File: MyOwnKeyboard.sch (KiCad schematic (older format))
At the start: 346 parts

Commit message: Assigned switches Romer-G footprint
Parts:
- SW1, SW10, SW100, SW101, SW102, SW103, SW104, SW105, SW106, SW107, SW108, SW109, SW11, SW110, SW111, SW112, SW113, SW114, SW115, SW116, SW117, SW118, SW119, SW12, SW120, SW121, SW122, SW123, SW124, SW125, SW126, SW127, SW128, SW129, SW13, SW130, SW131, SW132, SW133, SW134, SW135, SW136, SW137, SW138, SW139, SW14, SW140, SW141, SW142, SW143, SW144, SW145, SW146, SW147, SW148, SW149, SW15, SW150, SW151, SW152, SW153, SW154, SW155, SW156, SW157, SW158, SW159, SW16, SW160, SW161, SW162, SW163, SW164, SW165, SW166, SW167, SW168, SW169, SW17, SW170, SW171, SW172, SW173, SW174, SW175, SW176, SW177, SW178, SW179, SW18, SW180, SW181, SW182, SW183, SW184, SW185, SW186, SW187, SW188, SW189, SW19, SW190, SW191, SW192, SW193, SW194, SW195, SW196, SW197, SW198, SW199, SW2, SW20, SW200, SW201, SW202, SW203, SW204, SW205, SW206, SW207, SW208, SW209, SW21, SW210, SW211, SW212, SW213, SW214, SW215, SW216, SW217, SW218, SW219, SW22, SW220, SW221, SW222, SW223, SW224, SW225, SW226, SW227, SW228, SW23, SW24, SW25, SW26, SW27, SW28, SW29, SW3, SW30, SW31, SW32, SW33, SW34, SW35, SW36, SW37, SW38, SW39, SW4, SW40, SW41, SW42, SW43, SW44, SW45, SW46, SW47, SW48, SW49, SW5, SW50, SW51, SW52, SW53, SW54, SW55, SW56, SW57, SW58, SW59, SW6, SW60, SW61, SW62, SW63, SW64, SW65, SW66, SW67, SW68, SW69, SW7, SW70, SW71, SW72, SW73, SW74, SW75, SW76, SW77, SW78, SW79, SW8, SW80, SW81, SW82, SW83, SW84, SW85, SW86, SW87, SW88, SW89, SW9, SW90, SW91, SW92, SW93, SW94, SW95, SW96, SW97, SW98, SW99: renamed from SW?; footprint (none) -> MyOwnKeyboard:RomerG
- gave numbers to parts that had none: 118

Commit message: Migrate to the ATMega164
Why use IO expanders when you can just get more pins. It still turns out ~$3 cheaper.
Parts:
- removed SW1, SW10, SW100, SW101, SW102, SW103, SW104, SW105, SW106, SW107, SW108, SW109, SW11, SW110, SW111, SW112, SW113, SW114, SW12, SW13, SW14, SW15, SW16, SW17, SW18, SW19, SW2, SW20, SW21, SW22, SW23, SW24, SW25, SW26, SW27, SW28, SW29, SW3, SW30, SW31, SW32, SW33, SW34, SW35, SW36, SW37, SW38, SW39, SW4, SW40, SW41, SW42, SW43, SW44, SW45, SW46, SW47, SW48, SW49, SW5, SW50, SW51, SW52, SW53, SW54, SW55, SW56, SW57, SW58, SW59, SW6, SW60, SW61, SW62, SW63, SW64, SW65, SW66, SW67, SW68, SW69, SW7, SW70, SW71, SW72, SW73, SW74, SW75, SW76, SW77, SW78, SW79, SW8, SW80, SW81, SW82, SW83, SW84, SW85, SW86, SW87, SW88, SW89, SW9, SW90, SW91, SW92, SW93, SW94, SW95, SW96, SW97, SW98, SW99: SW_SPST, MyOwnKeyboard:RomerG, symbol Switch:SW_SPST
- removed U1: ATtiny85-20PU, Package_DIP:DIP-8_W7.62mm, symbol MCU_Microchip_ATtiny:ATtiny85-20PU
- removed U2, U3: MCP23017_SP, Package_DIP:DIP-28_W7.62mm, symbol Interface_Expansion:MCP23017_SP
- added C1, C2: 30pF, symbol Device:CP1
- added D115, D116, D117: LED, symbol Device:LED
- added Q1: 2N7000, Package_TO_SOT_THT:TO-92_Inline, symbol Transistor_FET:2N7000
- added R1: 100, symbol Device:R
- added R2: 100k, symbol Device:R
- added R3, R4, R5: 150, symbol Device:R
- added U1: ATmega164P-20PU, Package_DIP:DIP-40_W15.24mm, symbol MCU_Microchip_ATmega:ATmega164P-20PU
- added Y1: 20MHz, Crystal:Crystal_HC49-U_Horizontal, symbol Device:Crystal
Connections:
- net labels added: Counter2A-PWM
- net labels removed: SCL, SDA
- wire segments 1151 -> 616
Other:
- note removed: "I2C"
- note removed: "PS/2"
- moved on the sheet: J1

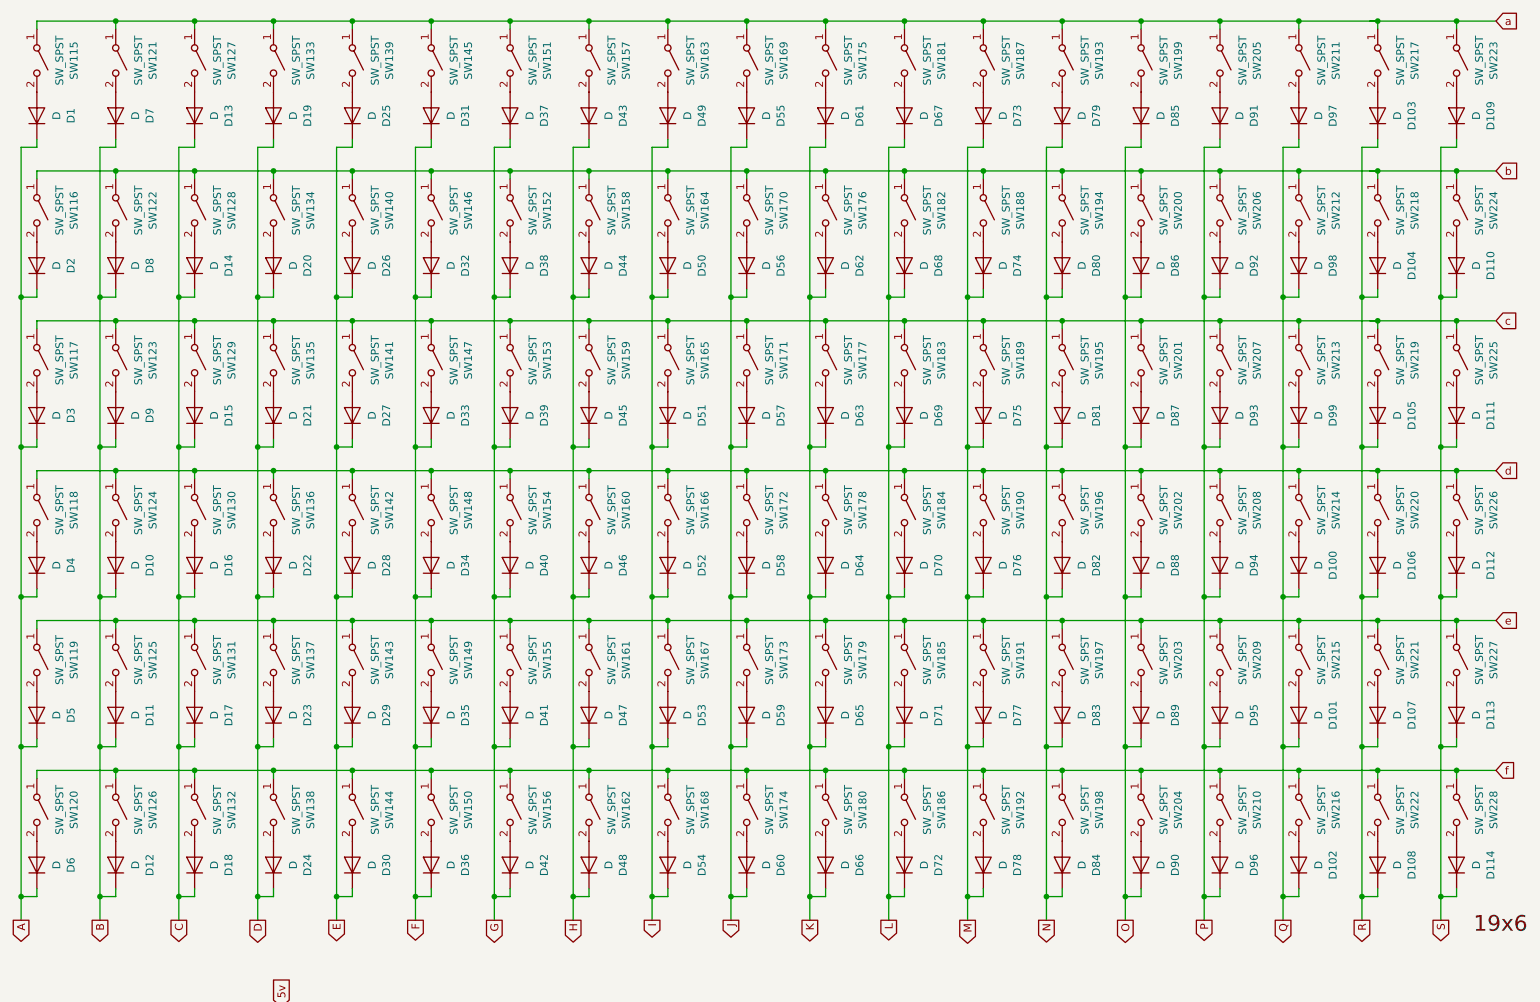
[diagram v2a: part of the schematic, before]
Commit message: Add LED and assign footprints
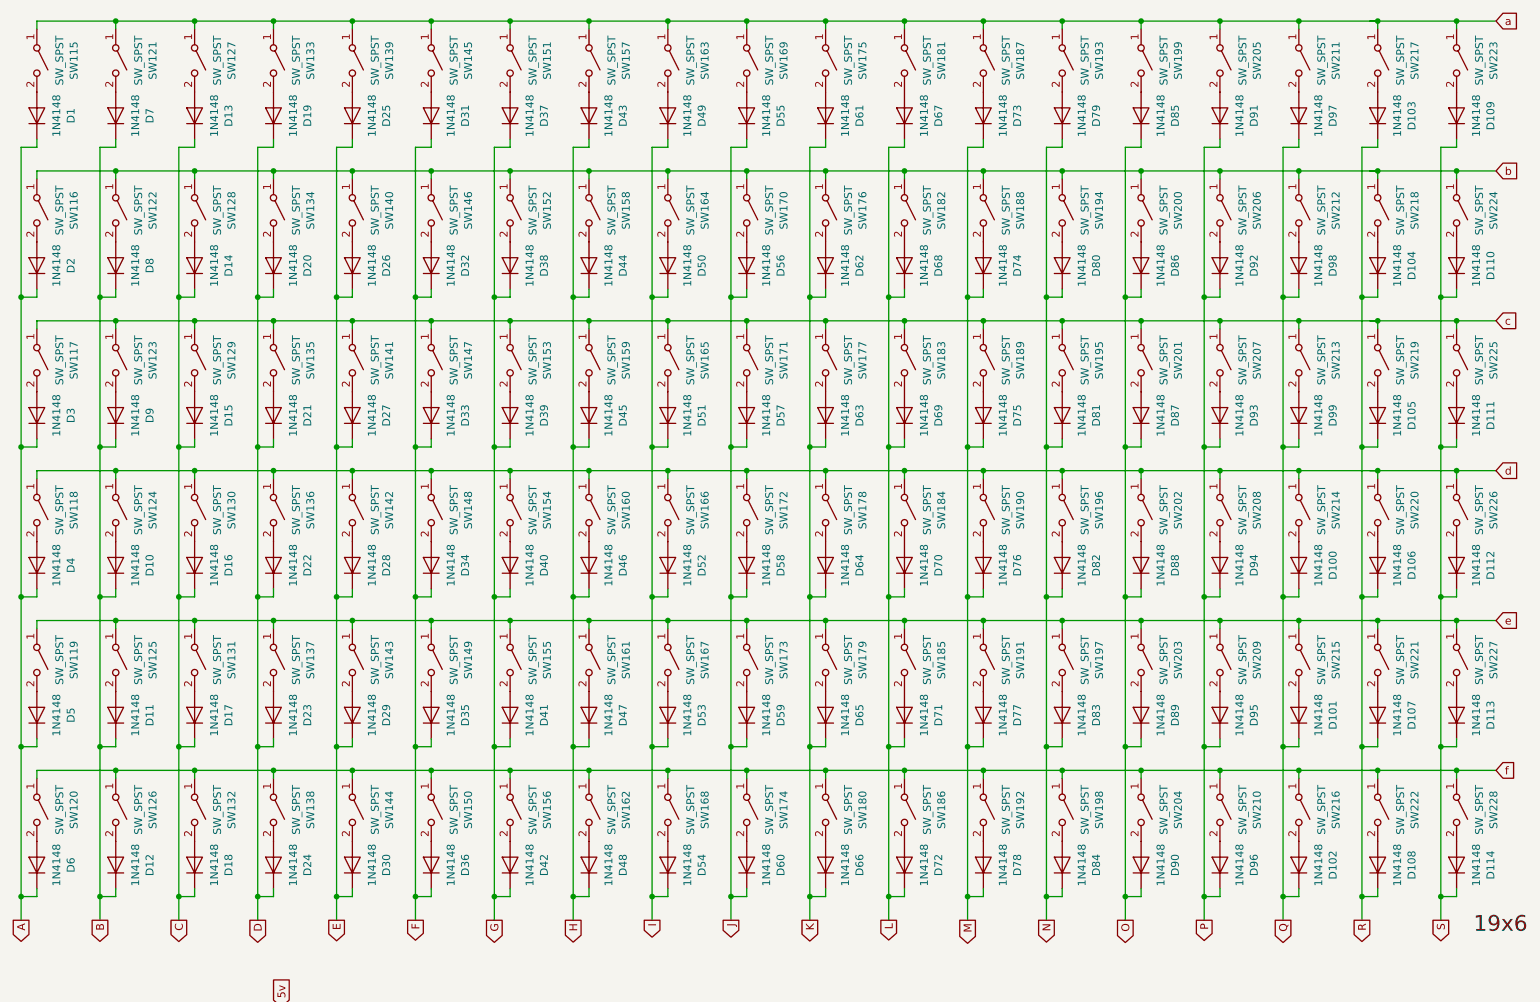
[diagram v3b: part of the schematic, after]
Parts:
- D1, D10, D100, D101, D102, D103, D104, D105, D106, D107, D108, D109, D11, D110, D111, D112, D113, D114, D12, D13, D14, D15, D16, D17, D18, D19, D2, D20, D21, D22, D23, D24, D25, D26, D27, D28, D29, D3, D30, D31, D32, D33, D34, D35, D36, D37, D38, D39, D4, D40, D41, D42, D43, D44, D45, D46, D47, D48, D49, D5, D50, D51, D52, D53, D54, D55, D56, D57, D58, D59, D6, D60, D61, D62, D63, D64, D65, D66, D67, D68, D69, D7, D70, D71, D72, D73, D74, D75, D76, D77, D78, D79, D8, D80, D81, D82, D83, D84, D85, D86, D87, D88, D89, D9, D90, D91, D92, D93, D94, D95, D96, D97, D98, D99: value D -> 1N4148; footprint (none) -> Diode_THT:D_DO-35_SOD27_P7.62mm_Horizontal
- D115, D116, D117: footprint (none) -> MyOwnKeyboard:158301250
- R1, R2, R3, R4, R5: footprint (none) -> Resistor_SMD:R_0805_2012Metric_Pad1.15x1.40mm_HandSolder

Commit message: Add per-key LEDs, basic PCB layout
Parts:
- added D118, D119, D120, D121, D122, D123, D124, D125, D126, D127, D128, D129, D130, D131, D132, D133, D134, D135, D136, D137, D138, D139, D140, D141, D142, D143, D144, D145, D146, D147, D148, D149, D150, D151, D152, D153, D154, D155, D156, D157, D158, D159, D160, D161, D162, D163, D164, D165, D166, D167, D168, D169, D170, D171, D172, D173, D174, D175, D176, D177, D178, D179, D180, D181, D182, D183, D184, D185, D186, D187, D188, D189, D190, D191, D192, D193, D194, D195, D196, D197, D198, D199, D200, D201, D202, D203, D204, D205, D206, D207, D208, D209, D210, D211, D212, D213, D214, D215, D216, D217, D218, D219, D220, D221, D222, D223, D224, D225, D226, D227, D228: LED, MyOwnKeyboard:158301250, symbol Device:LED
- added R10, R100, R101, R102, R103, R104, R105, R106, R107, R108, R109, R11, R110, R111, R112, R113, R114, R115, R116, R12, R13, R14, R15, R16, R17, R18, R19, R20, R21, R22, R23, R24, R25, R26, R27, R28, R29, R30, R31, R32, R33, R34, R35, R36, R37, R38, R39, R40, R41, R42, R43, R44, R45, R46, R47, R48, R49, R50, R51, R52, R53, R54, R55, R56, R57, R58, R59, R6, R60, R61, R62, R63, R64, R65, R66, R67, R68, R69, R7, R70, R71, R72, R73, R74, R75, R76, R77, R78, R79, R8, R80, R81, R82, R83, R84, R85, R86, R87, R88, R89, R9, R90, R91, R92, R93, R94, R95, R96, R97, R98, R99: 2.3k, Resistor_SMD:R_0805_2012Metric_Pad1.15x1.40mm_HandSolder, symbol Device:R
- R3, R4, R5: value 150 -> 2.3k
- renumbered D55 to D10, D30 to D100, D36 to D101, D42 to D102, D48 to D103, D54 to D104, D60 to D105, D66 to D106, D72 to D107, D78 to D108, D84 to D109, D61 to D11, D90 to D110, D96 to D111, D102 to D112, D108 to D113, D67 to D12, D73 to D13, D79 to D14, D85 to D15, D91 to D16, D97 to D17, D103 to D18, D109 to D19, D7 to D2, D2 to D20, D8 to D21, D14 to D22, D20 to D23, D26 to D24, D32 to D25, D38 to D26, D44 to D27, D50 to D28, D56 to D29, D13 to D3, D62 to D30, D68 to D31, D74 to D32, D80 to D33, D86 to D34, D92 to D35, D98 to D36, D104 to D37, D110 to D38, D3 to D39, D19 to D4, D9 to D40, D15 to D41, D21 to D42, D27 to D43, D33 to D44, D39 to D45, D45 to D46, D51 to D47, D57 to D48, D63 to D49, D25 to D5, D69 to D50, D75 to D51, D81 to D52, D87 to D53, D93 to D54, D99 to D55, D105 to D56, D111 to D57, D4 to D58, D10 to D59, D31 to D6, D16 to D60, D22 to D61, D28 to D62, D34 to D63, D40 to D64, D46 to D65, D52 to D66, D58 to D67, D64 to D68, D70 to D69, D37 to D7, D76 to D70, D82 to D71, D88 to D72, D94 to D73, D100 to D74, D106 to D75, D112 to D76, D5 to D77, D11 to D78, D17 to D79, D43 to D8, D23 to D80, D29 to D81, D35 to D82, D41 to D83, D47 to D84, D53 to D85, D59 to D86, D65 to D87, D71 to D88, D77 to D89, D49 to D9, D83 to D90, D89 to D91, D95 to D92, D101 to D93, D107 to D94, D113 to D95, D6 to D96, D12 to D97, D18 to D98, D24 to D99, SW115 to SW1, SW169 to SW10, SW144 to SW100, SW150 to SW101, SW156 to SW102, SW162 to SW103, SW168 to SW104, SW174 to SW105, SW180 to SW106, SW186 to SW107, SW192 to SW108, SW198 to SW109, SW175 to SW11, SW204 to SW110, SW210 to SW111, SW216 to SW112, SW222 to SW113, SW228 to SW114, SW181 to SW12, SW187 to SW13, SW193 to SW14, SW199 to SW15, SW205 to SW16, SW211 to SW17, SW217 to SW18, SW223 to SW19, SW121 to SW2, SW116 to SW20, SW122 to SW21, SW128 to SW22, SW134 to SW23, SW140 to SW24, SW146 to SW25, SW152 to SW26, SW158 to SW27, SW164 to SW28, SW170 to SW29, SW127 to SW3, SW176 to SW30, SW182 to SW31, SW188 to SW32, SW194 to SW33, SW200 to SW34, SW206 to SW35, SW212 to SW36, SW218 to SW37, SW224 to SW38, SW117 to SW39, SW133 to SW4, SW123 to SW40, SW129 to SW41, SW135 to SW42, SW141 to SW43, SW147 to SW44, SW153 to SW45, SW159 to SW46, SW165 to SW47, SW171 to SW48, SW177 to SW49, SW139 to SW5, SW183 to SW50, SW189 to SW51, SW195 to SW52, SW201 to SW53, SW207 to SW54, SW213 to SW55, SW219 to SW56, SW225 to SW57, SW118 to SW58, SW124 to SW59, SW145 to SW6, SW130 to SW60, SW136 to SW61, SW142 to SW62, SW148 to SW63, SW154 to SW64, SW160 to SW65, SW166 to SW66, SW172 to SW67, SW178 to SW68, SW184 to SW69, SW151 to SW7, SW190 to SW70, SW196 to SW71, SW202 to SW72, SW208 to SW73, SW214 to SW74, SW220 to SW75, SW226 to SW76, SW119 to SW77, SW125 to SW78, SW131 to SW79, SW157 to SW8, SW137 to SW80, SW143 to SW81, SW149 to SW82, SW155 to SW83, SW161 to SW84, SW167 to SW85, SW173 to SW86, SW179 to SW87, SW185 to SW88, SW191 to SW89, SW163 to SW9, SW197 to SW90, SW203 to SW91, SW209 to SW92, SW215 to SW93, SW221 to SW94, SW227 to SW95, SW120 to SW96, SW126 to SW97, SW132 to SW98, SW138 to SW99
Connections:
- net 5v: now also R3.1, R4.1, R5.1, R10.1, R100.1, R101.1, R102.1, R103.1, R104.1, R105.1, R106.1, R107.1, R108.1, R109.1, R11.1, R110.1, R111.1, R112.1, R113.1, R114.1, R115.1, R116.1, R12.1, R13.1, R14.1, R15.1, R16.1, R17.1, R18.1, R19.1, R20.1, R21.1, R22.1, R23.1, R24.1, R25.1, R26.1, R27.1, R28.1, R29.1, R30.1, R31.1, R32.1, R33.1, R34.1, R35.1, R36.1, R37.1, R38.1, R39.1, R40.1, R41.1, R42.1, R43.1, R44.1, R45.1, R46.1, R47.1, R48.1, R49.1, R50.1, R51.1, R52.1, R53.1, R54.1, R55.1, R56.1, R57.1, R58.1, R59.1, R6.1, R60.1, R61.1, R62.1, R63.1, R64.1, R65.1, R66.1, R67.1, R68.1, R69.1, R7.1, R70.1, R71.1, R72.1, R73.1, R74.1, R75.1, R76.1, R77.1, R78.1, R79.1, R8.1, R80.1, R81.1, R82.1, R83.1, R84.1, R85.1, R86.1, R87.1, R88.1, R89.1, R9.1, R90.1, R91.1, R92.1, R93.1, R94.1, R95.1, R96.1, R97.1, R98.1, R99.1; no longer R3.2, R4.2, R5.2
- net Counter2A-PWM: now also R1.1; no longer R1.2
- net at D115.1 (K), D116.1 (K), D117.1 (K)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: now also D118.1 (K), D119.1 (K), D120.1 (K), D121.1 (K), D122.1 (K), D123.1 (K), D124.1 (K), D125.1 (K), D126.1 (K), D127.1 (K), D128.1 (K), D129.1 (K), D130.1 (K), D131.1 (K), D132.1 (K), D133.1 (K), D134.1 (K), D135.1 (K), D136.1 (K), D137.1 (K), D138.1 (K), D139.1 (K), D140.1 (K), D141.1 (K), D142.1 (K), D143.1 (K), D144.1 (K), D145.1 (K), D146.1 (K), D147.1 (K), D148.1 (K), D149.1 (K), D150.1 (K), D151.1 (K), D152.1 (K), D153.1 (K), D154.1 (K), D155.1 (K), D156.1 (K), D157.1 (K), D158.1 (K), D159.1 (K), D160.1 (K), D161.1 (K), D162.1 (K), D163.1 (K), D164.1 (K), D165.1 (K), D166.1 (K), D167.1 (K), D168.1 (K), D169.1 (K), D170.1 (K), D171.1 (K), D172.1 (K), D173.1 (K), D174.1 (K), D175.1 (K), D176.1 (K), D177.1 (K), D178.1 (K), D179.1 (K), D180.1 (K), D181.1 (K), D182.1 (K), D183.1 (K), D184.1 (K), D185.1 (K), D186.1 (K), D187.1 (K), D188.1 (K), D189.1 (K), D190.1 (K), D191.1 (K), D192.1 (K), D193.1 (K), D194.1 (K), D195.1 (K), D196.1 (K), D197.1 (K), D198.1 (K), D199.1 (K), D200.1 (K), D201.1 (K), D202.1 (K), D203.1 (K), D204.1 (K), D205.1 (K), D206.1 (K), D207.1 (K), D208.1 (K), D209.1 (K), D210.1 (K), D211.1 (K), D212.1 (K), D213.1 (K), D214.1 (K), D215.1 (K), D216.1 (K), D217.1 (K), D218.1 (K), D219.1 (K), D220.1 (K), D221.1 (K), D222.1 (K), D223.1 (K), D224.1 (K), D225.1 (K), D226.1 (K), D227.1 (K), D228.1 (K)
- net at D117.2 (A): now also R5.2; no longer R5.1
- net at D116.2 (A): now also R4.2; no longer R4.1
- net at D115.2 (A): now also R3.2; no longer R3.1
- net at Q1.2 (G), R2.1: now also R1.2; no longer R1.1
- new net: D134.2 (A), R22.2
- new net: D153.2 (A), R41.2
- new net: D172.2 (A), R60.2
- new net: D191.2 (A), R79.2
- new net: D210.2 (A), R98.2
- new net: D135.2 (A), R23.2
- new net: D154.2 (A), R42.2
- new net: D173.2 (A), R61.2
- new net: D192.2 (A), R80.2
- new net: D211.2 (A), R99.2
- new net: D136.2 (A), R24.2
- new net: D155.2 (A), R43.2
- new net: D174.2 (A), R62.2
- new net: D193.2 (A), R81.2
- new net: D212.2 (A), R100.2
- new net: D118.2 (A), R6.2
- new net: D137.2 (A), R25.2
- new net: D156.2 (A), R44.2
- new net: D175.2 (A), R63.2
- new net: D194.2 (A), R82.2
- new net: D213.2 (A), R101.2
- new net: D119.2 (A), R7.2
- new net: D138.2 (A), R26.2
- new net: D157.2 (A), R45.2
- new net: D176.2 (A), R64.2
- new net: D195.2 (A), R83.2
- new net: D214.2 (A), R102.2
- new net: D120.2 (A), R8.2
- new net: D139.2 (A), R27.2
- new net: D158.2 (A), R46.2
- new net: D177.2 (A), R65.2
- new net: D196.2 (A), R84.2
- new net: D215.2 (A), R103.2
- new net: D121.2 (A), R9.2
- new net: D140.2 (A), R28.2
- new net: D159.2 (A), R47.2
- new net: D178.2 (A), R66.2
- new net: D197.2 (A), R85.2
- new net: D216.2 (A), R104.2
- new net: D122.2 (A), R10.2
- new net: D141.2 (A), R29.2
- new net: D160.2 (A), R48.2
- new net: D179.2 (A), R67.2
- new net: D198.2 (A), R86.2
- new net: D217.2 (A), R105.2
- new net: D123.2 (A), R11.2
- new net: D142.2 (A), R30.2
- new net: D161.2 (A), R49.2
- new net: D180.2 (A), R68.2
- new net: D199.2 (A), R87.2
- new net: D218.2 (A), R106.2
- new net: D124.2 (A), R12.2
- new net: D143.2 (A), R31.2
- new net: D162.2 (A), R50.2
- new net: D181.2 (A), R69.2
- new net: D200.2 (A), R88.2
- new net: D219.2 (A), R107.2
- new net: D125.2 (A), R13.2
- new net: D144.2 (A), R32.2
- new net: D163.2 (A), R51.2
- new net: D182.2 (A), R70.2
- new net: D201.2 (A), R89.2
- new net: D220.2 (A), R108.2
- new net: D126.2 (A), R14.2
- new net: D145.2 (A), R33.2
- new net: D164.2 (A), R52.2
- new net: D183.2 (A), R71.2
- new net: D202.2 (A), R90.2
- new net: D221.2 (A), R109.2
- new net: D127.2 (A), R15.2
- new net: D146.2 (A), R34.2
- new net: D165.2 (A), R53.2
- new net: D184.2 (A), R72.2
- new net: D203.2 (A), R91.2
- new net: D222.2 (A), R110.2
- new net: D128.2 (A), R16.2
- new net: D147.2 (A), R35.2
- new net: D166.2 (A), R54.2
- new net: D185.2 (A), R73.2
- new net: D204.2 (A), R92.2
- new net: D223.2 (A), R111.2
- new net: D129.2 (A), R17.2
- new net: D148.2 (A), R36.2
- new net: D167.2 (A), R55.2
- new net: D186.2 (A), R74.2
- new net: D205.2 (A), R93.2
- new net: D224.2 (A), R112.2
- new net: D130.2 (A), R18.2
- new net: D149.2 (A), R37.2
- new net: D168.2 (A), R56.2
- new net: D187.2 (A), R75.2
- new net: D206.2 (A), R94.2
- new net: D225.2 (A), R113.2
- new net: D131.2 (A), R19.2
- new net: D150.2 (A), R38.2
- new net: D169.2 (A), R57.2
- new net: D188.2 (A), R76.2
- new net: D207.2 (A), R95.2
- new net: D226.2 (A), R114.2
- new net: D132.2 (A), R20.2
- new net: D151.2 (A), R39.2
- new net: D170.2 (A), R58.2
- new net: D189.2 (A), R77.2
- new net: D208.2 (A), R96.2
- new net: D227.2 (A), R115.2
- new net: D133.2 (A), R21.2
- new net: D152.2 (A), R40.2
- new net: D171.2 (A), R59.2
- new net: D190.2 (A), R78.2
- new net: D209.2 (A), R97.2
- new net: D228.2 (A), R116.2
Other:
- moved on the sheet: C1, C2, D1, D10, D100, D101, D102, D103, D104, D105, D106, D107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

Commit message: Add NUM/CAPSLOCK indicators, finalise components
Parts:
- added D229: NUMLOCK, MyOwnKeyboard:158301250, symbol Device:LED
- added D230: CAPSLOCK, MyOwnKeyboard:158301250, symbol Device:LED
- added R117, R118: 2.3k, Resistor_SMD:R_0805_2012Metric_Pad1.15x1.40mm_HandSolder, symbol Device:R
- C1, C2: footprint (none) -> Capacitor_SMD:C_0805_2012Metric_Pad1.15x1.40mm_HandSolder
- J1: footprint (none) -> Connector_PinHeader_1.27mm:PinHeader_1x06_P1.27mm_Vertical
- Q1: value 2N7000 -> RFD14N05L; footprint Package_TO_SOT_THT:TO-92_Inline -> Package_TO_SOT_THT:TO-251-3-1EP_Horizontal_TabDown
- U1: symbol MCU_Microchip_ATmega:ATmega164P-20PU -> MyOwnKeyboard-rescue:ATmega164P-20PU-MCU_Microchip_ATmega
- Y1: footprint Crystal:Crystal_HC49-U_Horizontal -> Crystal:Crystal_HC49-U_Vertical
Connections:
- net 5v: now also D229.2 (A), D230.2 (A)
- net at U1.26 (PC4): now also R117.1
- net at U1.27 (PC5): now also R118.1
- new net: D229.1 (K), R117.2
- new net: D230.1 (K), R118.2
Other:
- moved on the sheet: J1
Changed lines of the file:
@@
 EESchema Schematic File Version 4
+LIBS:MyOwnKeyboard-cache
 EELAYER 30 0
 EELAYER END
@@
 f
 $Comp
-L MCU_Microchip_ATmega:ATmega164P-20PU U1
+L MyOwnKeyboard-rescue:ATmega164P-20PU-MCU_Microchip_ATmega U1
 U 1 1 5F6749FA
 P 2250 13900
@@
 	1    0    0    -1
 $EndComp
-Text Label 3050 14500 0    50   ~ 0
+Text Label 3050 14600 0    50   ~ 0
 Clk
-Text Label 3050 14700 0    50   ~ 0
+Text Label 3050 14800 0    50   ~ 0
 Data
 $Comp
 L Connector:Mini-DIN-6 J1
 U 1 1 6054BCBD
-P 3800 14600
-F 0 "J1" H 4000 14850 50  0000 C CNN
-F 1 "Mini-DIN-6" H 3550 14850 50  0000 C CNN
-F 2 "" H 3800 14600 50  0001 C CNN
-F 3 "http://service.powerdynamics.com/ec/Catalog17/Section%2011.pdf" H 3800 14600 50  0001 C CNN
-	1    3800 14600
+P 3800 14700
+F 0 "J1" H 4000 14950 50  0000 C CNN
+F 1 "Mini-DIN-6" H 3550 14950 50  0000 C CNN
+F 2 "Connector_PinHeader_1.27mm:PinHeader_1x06_P1.27mm_Vertical" H 3800 14700 50  0001 C CNN
+F 3 "http://service.powerdynamics.com/ec/Catalog17/Section%2011.pdf" H 3800 14700 50  0001 C CNN
+	1    3800 14700
 	-1   0    0    -1
 $EndComp
-Text GLabel 3500 14600 0    50   BiDi ~ 0
+Text GLabel 3500 14700 0    50   BiDi ~ 0
 GND
-NoConn ~ 4100 14700
-NoConn ~ 4100 14500
-Text GLabel 4100 14600 2    50   Output ~ 0
+NoConn ~ 4100 14800
+NoConn ~ 4100 14600
+Text GLabel 4100 14700 2    50   Output ~ 0
 5v
 $Comp
@@
 F 0 "Y1" V 950 12350 50  0000 L CNN
 F 1 "20MHz" V 950 12550 50  0000 L CNN
-F 2 "Crystal:Crystal_HC49-U_Horizontal" H 1100 12500 50  0001 C CNN
+F 2 "Crystal:Crystal_HC49-U_Vertical" H 1100 12500 50  0001 C CNN
 F 3 "~" H 1100 12500 50  0001 C CNN
 	1    1100 12500
@@
 U 1 1 60774F83
 P 850 12250
-F 0 "C1" V 700 12200 50  0000 C CNN
+F 0 "C1" V 700 12150 50  0000 C CNN
 F 1 "30pF" V 700 12350 50  0000 C CNN
-F 2 "" H 850 12250 50  0001 C CNN
+F 2 "Capacitor_SMD:C_0805_2012Metric_Pad1.15x1.40mm_HandSolder" H 850 12250 50  0001 C CNN
 F 3 "~" H 850 12250 50  0001 C CNN
 	1    850  12250
@@
 U 1 1 60776852
 P 850 12750
-F 0 "C2" V 1000 12700 50  0000 C CNN
+F 0 "C2" V 1000 12650 50  0000 C CNN
 F 1 "30pF" V 1000 12850 50  0000 C CNN
-F 2 "" H 850 12750 50  0001 C CNN
+F 2 "Capacitor_SMD:C_0805_2012Metric_Pad1.15x1.40mm_HandSolder" H 850 12750 50  0001 C CNN
 F 3 "~" H 850 12750 50  0001 C CNN
 	1    850  12750
@@
 P 4500 15100
 F 0 "Q1" H 4704 15146 50  0000 L CNN
-F 1 "2N7000" H 4704 15055 50  0000 L CNN
-F 2 "Package_TO_SOT_THT:TO-92_Inline" H 4700 15025 50  0001 L CIN
+F 1 "RFD14N05L" H 4704 15055 50  0000 L CNN
+F 2 "Package_TO_SOT_THT:TO-251-3-1EP_Horizontal_TabDown" H 4700 15025 50  0001 L CIN
 F 3 "https://www.fairchildsemi.com/datasheets/2N/2N7000.pdf" H 4500 15100 50  0001 L CNN
 	1    4500 15100
@@
 	3900 15100 4200 15100
 Wire Wire Line
-	2850 14700 3500 14700
-Wire Wire Line
-	2850 14600 3000 14600
-Wire Wire Line
-	3000 14600 3000 14500
-Wire Wire Line
-	3000 14500 3500 14500
-Wire Wire Line
 	4600 14900 4600 11650
 $Comp
@@
 	1    0    0    -1
 $EndComp
+$Comp
+L Device:LED D229
+U 1 1 5EE7CE59
+P 4000 13650
+F 0 "D229" H 4150 13500 50  0000 C CNN
+F 1 "NUMLOCK" H 3825 13500 50  0000 C CNN
+F 2 "MyOwnKeyboard:158301250" H 4000 13650 50  0001 C CNN
+F 3 "~" H 4000 13650 50  0001 C CNN
+	1    4000 13650
+	1    0    0    1
+$EndComp
+$Comp
+L Device:LED D230
+U 1 1 5EE8076E
+P 4000 13950
+F 0 "D230" H 4150 14050 50  0000 C CNN
+F 1 "CAPSLOCK" H 3825 14050 50  0000 C CNN
+F 2 "MyOwnKeyboard:158301250" H 4000 13950 50  0001 C CNN
+F 3 "~" H 4000 13950 50  0001 C CNN
+	1    4000 13950
+	1    0    0    1
+$EndComp
+$Comp
+L Device:R R117
+U 1 1 5EE84056
+P 3500 13650
+F 0 "R117" V 3325 13650 50  0000 C CNN
+F 1 "2.3k" V 3400 13650 50  0000 C CNN
+F 2 "Resistor_SMD:R_0805_2012Metric_Pad1.15x1.40mm_HandSolder" V 3430 13650 50  0001 C CNN
+F 3 "~" H 3500 13650 50  0001 C CNN
+	1    3500 13650
+	0    -1   1    0
+$EndComp
+$Comp
+L Device:R R118
+U 1 1 5EE86968
+P 3500 13950
+F 0 "R118" V 3325 13950 50  0000 C CNN
+F 1 "2.3k" V 3400 13950 50  0000 C CNN
+F 2 "Resistor_SMD:R_0805_2012Metric_Pad1.15x1.40mm_HandSolder" V 3430 13950 50  0001 C CNN
+F 3 "~" H 3500 13950 50  0001 C CNN
+	1    3500 13950
+	0    -1   1    0
+$EndComp
+Wire Wire Line
+	3300 14500 3300 13950
+Wire Wire Line
+	3300 13950 3350 13950
+Wire Wire Line
+	3350 13650 3250 13650
+Wire Wire Line
+	3250 13650 3250 14400
+Text GLabel 4300 13800 2    50   Input ~ 0
+5v
+Wire Wire Line
+	4150 13650 4200 13650
+Wire Wire Line
+	4200 13650 4200 13800
+Wire Wire Line
+	4200 13950 4150 13950
+Wire Wire Line
+	4300 13800 4200 13800
+Connection ~ 4200 13800
+Wire Wire Line
+	4200 13800 4200 13950
+Wire Wire Line
+	2850 14600 3500 14600
+Wire Wire Line
+	2950 14800 2950 14700
+Wire Wire Line
+	2950 14700 2850 14700
+Wire Wire Line
+	2950 14800 3500 14800
+Wire Wire Line
+	2850 14500 3300 14500
+Wire Wire Line
+	2850 14400 3250 14400
+Wire Wire Line
+	3650 13650 3850 13650
+Wire Wire Line
+	3850 13950 3650 13950
 $EndSCHEMATC

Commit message: Removed crystal, finalised design
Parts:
- removed C1, C2: 30pF, Capacitor_SMD:C_0805_2012Metric_Pad1.15x1.40mm_HandSolder, symbol Device:CP1
- removed Y1: 20MHz, Crystal:Crystal_HC49-U_Vertical, symbol Device:Crystal
- U1: symbol MyOwnKeyboard-rescue:ATmega164P-20PU-MCU_Microchip_ATmega -> MyOwnKeyboard-rescue:ATmega164P-20PU-MCU_Microchip_ATmega-MyOwnKeyboard-rescue
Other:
- moved on the sheet: D229, D230, J1, R117, R118, U1
